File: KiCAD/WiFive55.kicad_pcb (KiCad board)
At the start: 2 copper layers, 45.7 x 47.6 mm, 53 parts, among them J2 Switched Output, J3 Breadboard, J4 Grounds, J5 555-esque, K1 FINDER-36.11, Q1 BS170, Q2 IRF540N, Q5 BC557, SW3 PRG, SW6 RST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

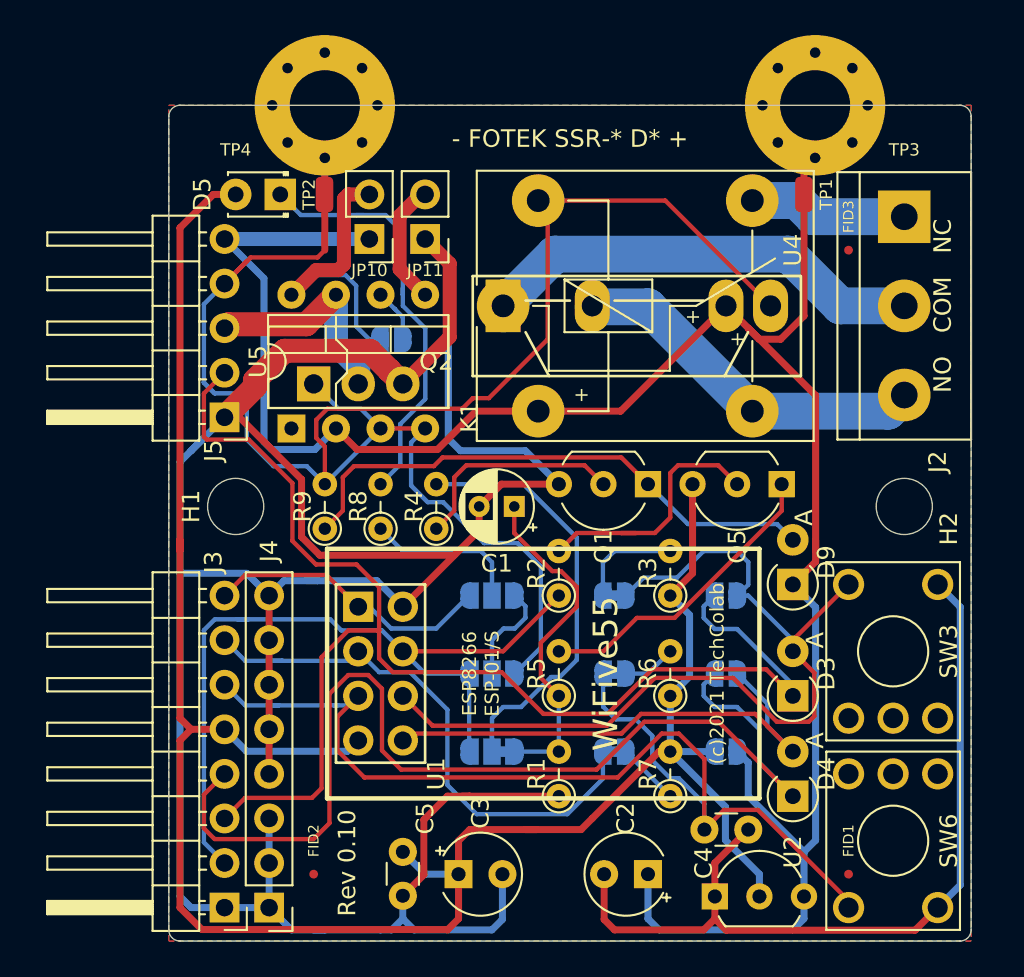
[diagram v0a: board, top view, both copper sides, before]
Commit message: update PCB for multiple SSR/RLA options
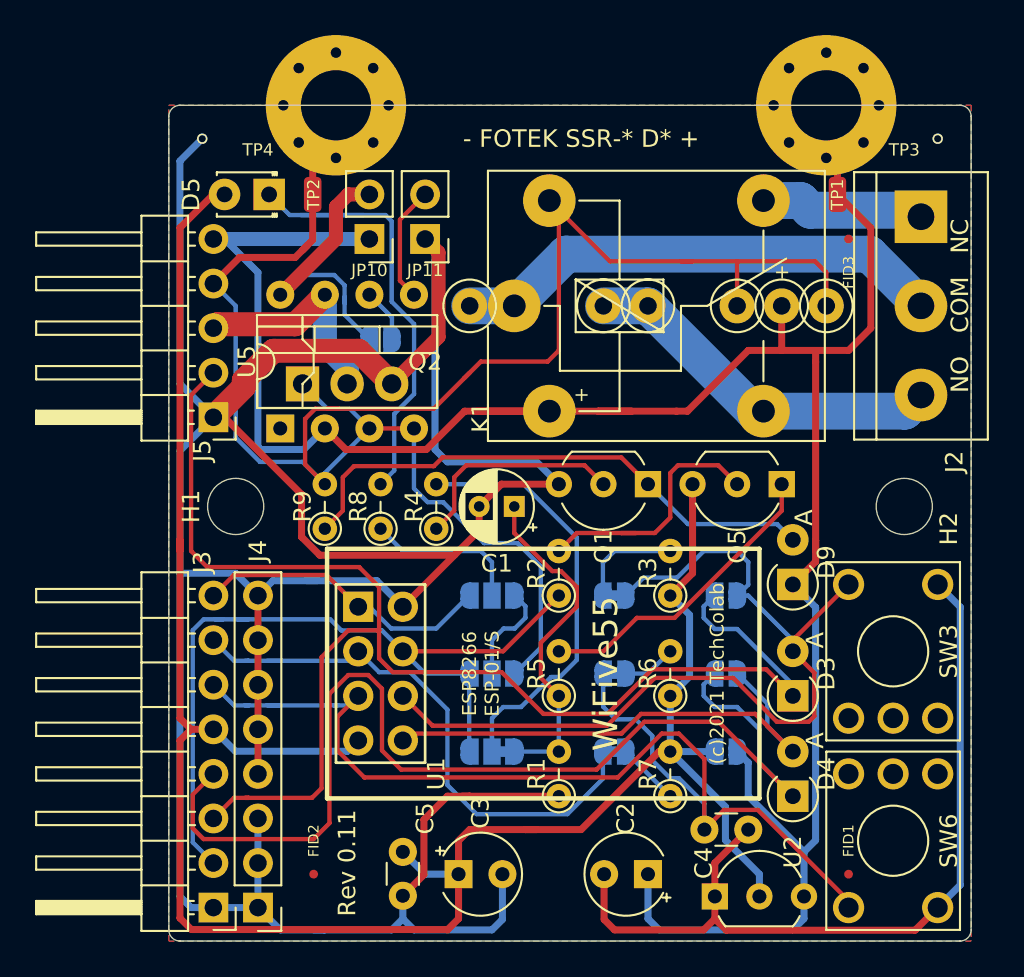
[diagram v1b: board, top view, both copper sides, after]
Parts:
- removed U4: S102S02, Package_SIP:SIP4_Sharp-SSR_P7.62mm_Straight
- added  : TestPoint_Loop_D1.80mm_Drill1.0mm_Beaded, TestPoint:TestPoint_Loop_D1.80mm_Drill1.0mm_Beaded, F.Cu at (137.8, 59.7)
- added  : TestPoint_Loop_D1.80mm_Drill1.0mm_Beaded, TestPoint:TestPoint_Loop_D1.80mm_Drill1.0mm_Beaded, F.Cu at (135.3, 59.7)
- added  : TestPoint_Loop_D1.80mm_Drill1.0mm_Beaded, TestPoint:TestPoint_Loop_D1.80mm_Drill1.0mm_Beaded, F.Cu at (132.7, 59.7)
- added  : TestPoint_Loop_D1.80mm_Drill1.0mm_Beaded, TestPoint:TestPoint_Loop_D1.80mm_Drill1.0mm_Beaded, F.Cu at (127.6, 59.7)
- added  : TestPoint_Loop_D1.80mm_Drill1.0mm_Beaded, TestPoint:TestPoint_Loop_D1.80mm_Drill1.0mm_Beaded, F.Cu at (125.1, 59.7)
- added  : TestPoint_Loop_D1.80mm_Drill1.0mm_Beaded, TestPoint:TestPoint_Loop_D1.80mm_Drill1.0mm_Beaded, F.Cu at (117.5, 59.7)
- moved TP1 1.91 mm to (138.4, 53.3)
- moved J2 0.95 mm to (143.2, 54.6)
- moved TP2 0.67 mm to (108.6, 53.3)
- moved D5 0.64 mm to (106.0, 53.3)
- moved J4 0.64 mm to (105.4, 94.0)
- moved K1 0.64 mm to (120.0, 59.7)
- moved TP4 0.64 mm to (109.9, 48.3)
- moved FID3 0.63 mm to (139.1, 55.9)
- moved J3 0.63 mm to (102.9, 94.0)
- moved J5 0.63 mm to (102.9, 66.0)
- moved Q2 0.63 mm to (108.0, 64.1)
- moved TP3 0.63 mm to (137.8, 48.3)
- moved U5 0.63 mm to (106.7, 66.7)
- moved JP12 0.62 mm to (112.4, 61.6)
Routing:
- net GND: track 219.1 -> 235.8 mm, vias 0 -> 2
- net +VDC: track 124.1 -> 134.5 mm
- net /!OUT: track 105.6 -> 114.3 mm
- net /!TRIGGER: track 76.7 -> 80.2 mm
- net Net-(D5-Pad1): track 24.6 -> 27.5 mm
- net /COM: track 25.3 -> 28.2 mm
- net /GPIO2: track 45.7 -> 47.6 mm
- net /ENABLE: track 31.8 -> 32.7 mm
- net /!RESET: track 64.5 -> 65.3 mm
- net /RX: track 62.9 -> 63.5 mm
- net Net-(JP10-Pad2): track 17.4 -> 16.9 mm
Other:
- board text added: "Rev 0.11"
- board text removed: "Rev 0.10"

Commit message: PCB v0.12
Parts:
- moved JP12 1.05 mm to (111.3, 61.6)
- moved Q2 0.50 mm to (107.5, 64.1)
- moved U5 0.50 mm to (106.2, 66.7)
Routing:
- net GND: track 235.8 -> 229.6 mm, vias 2 -> 4
- net /!OUT: track 114.3 -> 117.7 mm
- net Net-(JP11-Pad2): track 6.64 -> 7.44 mm
- net Net-(JP10-Pad2): track 16.9 -> 17.6 mm
- net +VDC: track 134.5 -> 135.1 mm
- net /OUT: track 12.7 -> 12.2 mm
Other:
- board text added: "Rev 0.12"
- board text removed: "Rev 0.11"

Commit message: Rev. 0.13 PCB
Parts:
- turned TP3 to 22.5 degrees
- turned TP4 to 22.5 degrees
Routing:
- net /NC: track 9.36 -> 11.0 mm
- net Net-(JP10-Pad2): track 17.6 -> 16.1 mm
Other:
- board text added: "N.ch sdg"
- board text added: "Notes: Relay/SSR upto 4A @ upto 250Vac* MOSFET upto 3A @ upto 100Vdc* Opto-Isolator upto 1.5A @ upto 15Vdc *with a polymer coating or 30V with bare traces."
- board text added: "Rev 0.13"
- board text removed: "Rev 0.12"
